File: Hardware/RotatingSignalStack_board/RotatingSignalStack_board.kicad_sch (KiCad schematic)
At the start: 42 parts, among them J1 8P8C_LED_Shielded, Q9 Q_PMOS_DGS, SW1 SW_Push, SW2 SW_Push, U1 OKI, U3 Teensy4.1_DEV-16771, U4 TSR_1-2450, U5 LSM303C

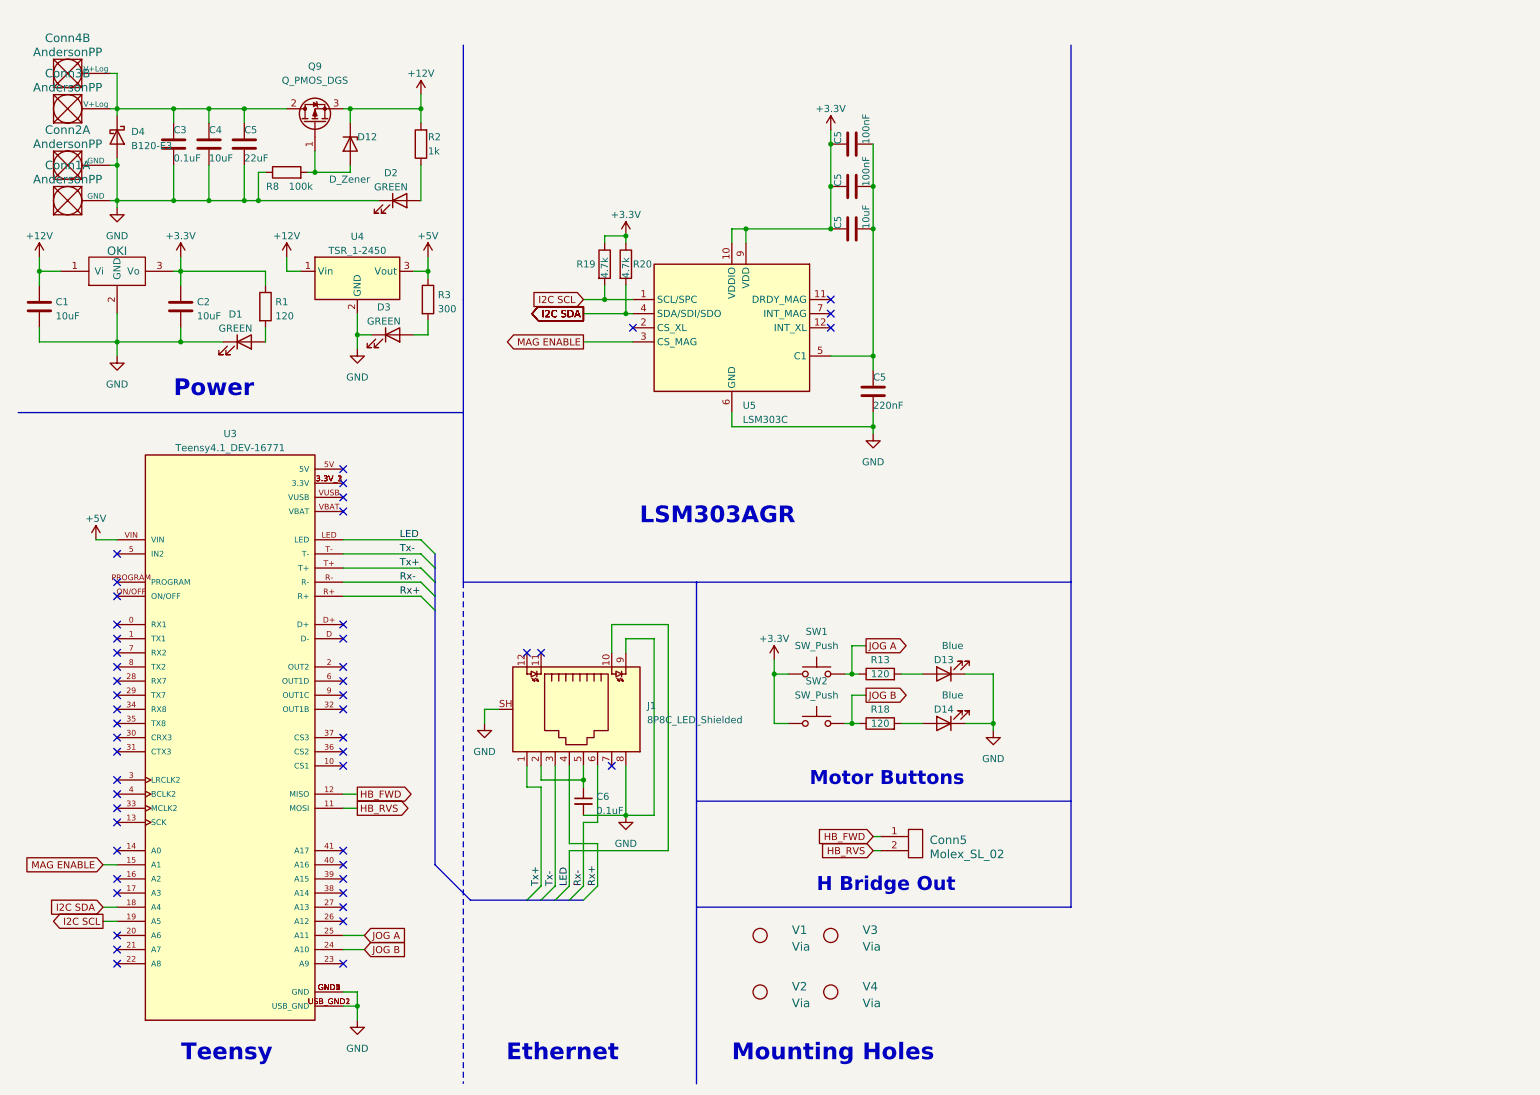
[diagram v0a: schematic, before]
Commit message: schematic changes, ethernet bus del, still have anderson issues, changed so VDDIO and VDD for compass chip are controlled by teensy outputs for startup seq to be possbile
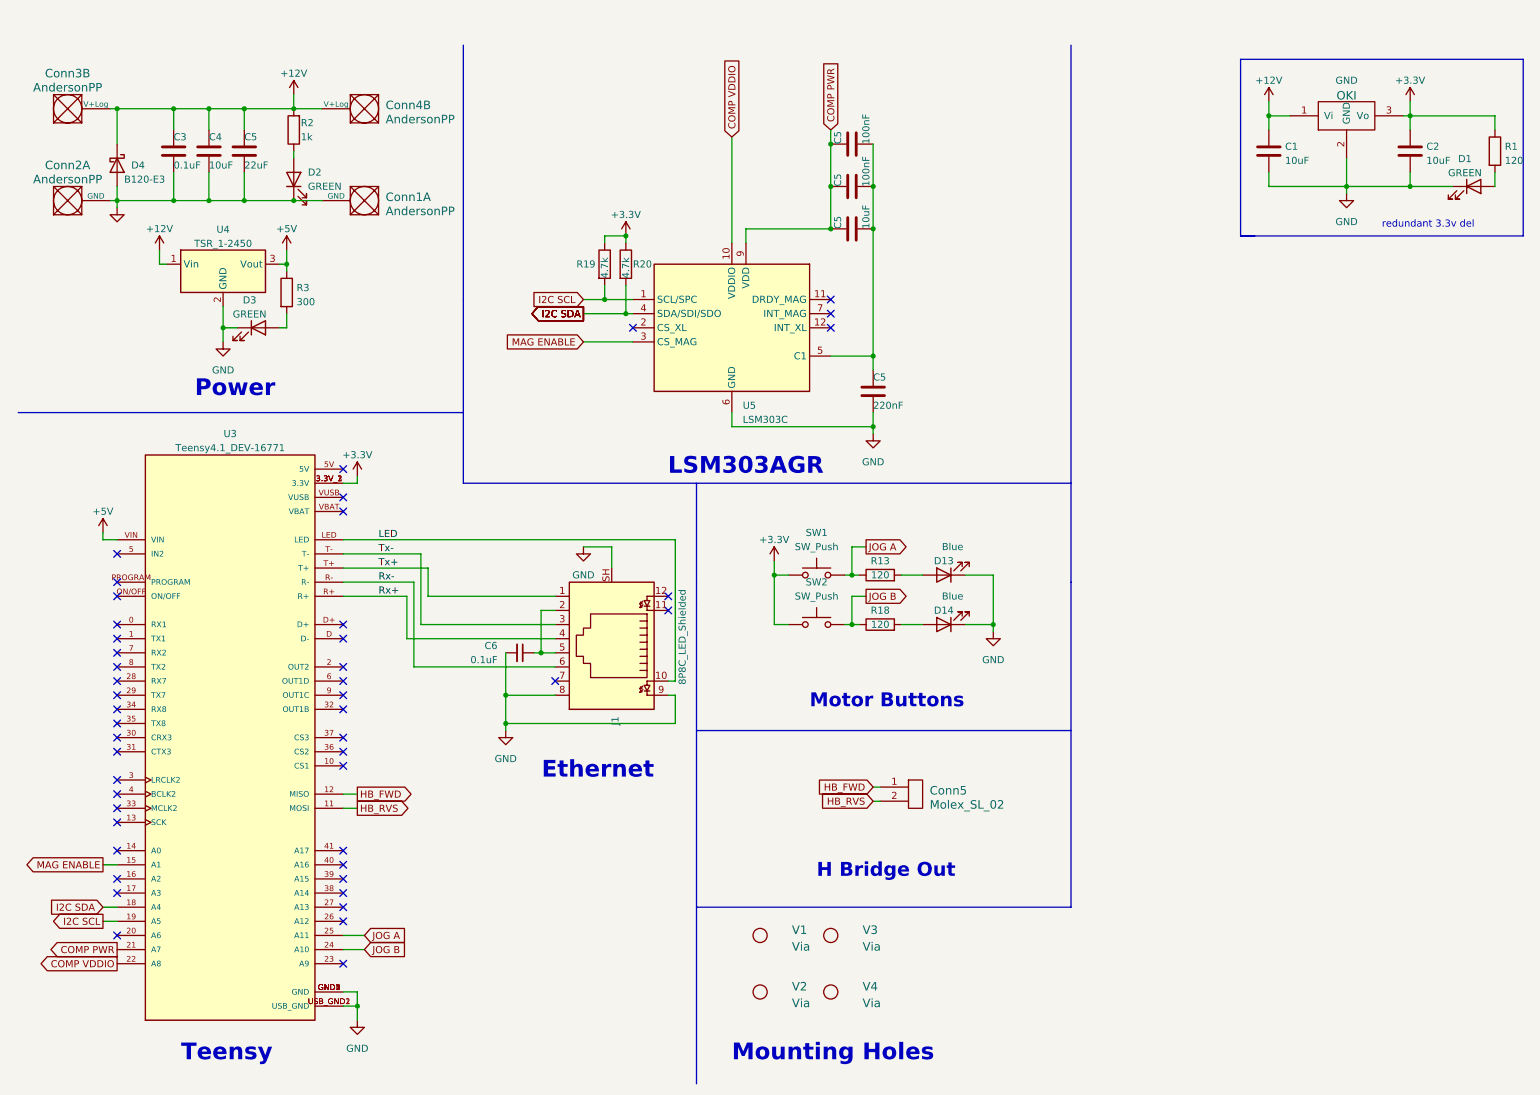
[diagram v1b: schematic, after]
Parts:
- removed D12: D_Zener, Package_TO_SOT_SMD:SOT-23-3, symbol Device:D_Zener
- removed Q9: Q_PMOS_DGS, Package_TO_SOT_SMD:TO-252-3_TabPin2, symbol Device:Q_PMOS_GDS
- removed R8: 100k, Resistor_SMD:R_0603_1608Metric_Pad0.98x0.95mm_HandSolder, symbol Device:R
- J1: footprint (none) -> MRDT_Connectors:RJ45_Teensy
- U3: footprint MODULE_DEV-16771 -> MRDT_Shields:Teensy_4_1_Ethernet
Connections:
- net +12V: now also C3.1, C4.1, C5.1, Conn3.2 (V+Log), Conn4.2 (V+Log), D4.1 (K)
- net +3.3V: now also U3.3.3V_1 (3.3V), U3.3.3V_2 (3.3V), U3.3.3V_3 (3.3V); no longer C5.1, C5.1, C5.1, U5.10 (VDDIO), U5.9 (VDD)
- net COMP PWR: now reaches U3.21 (A7)
- net COMP PWR: now also C5.1, C5.1, C5.1, U5.9 (VDD)
- net COMP VDDIO: now reaches U3.22 (A8)
- net COMP VDDIO: now also U5.10 (VDDIO)
- no-connect marks 50 -> 47
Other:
- note added: "redundant 3.3v del"
- moved on the sheet: C1, C2, C3, C4, C5, C6, Conn1A, Conn2A, Conn4B, Conn5, D1, D13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

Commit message: first update of changes from schem review, changes need double checked. BOM is generated in /manufacturing but needs filled out
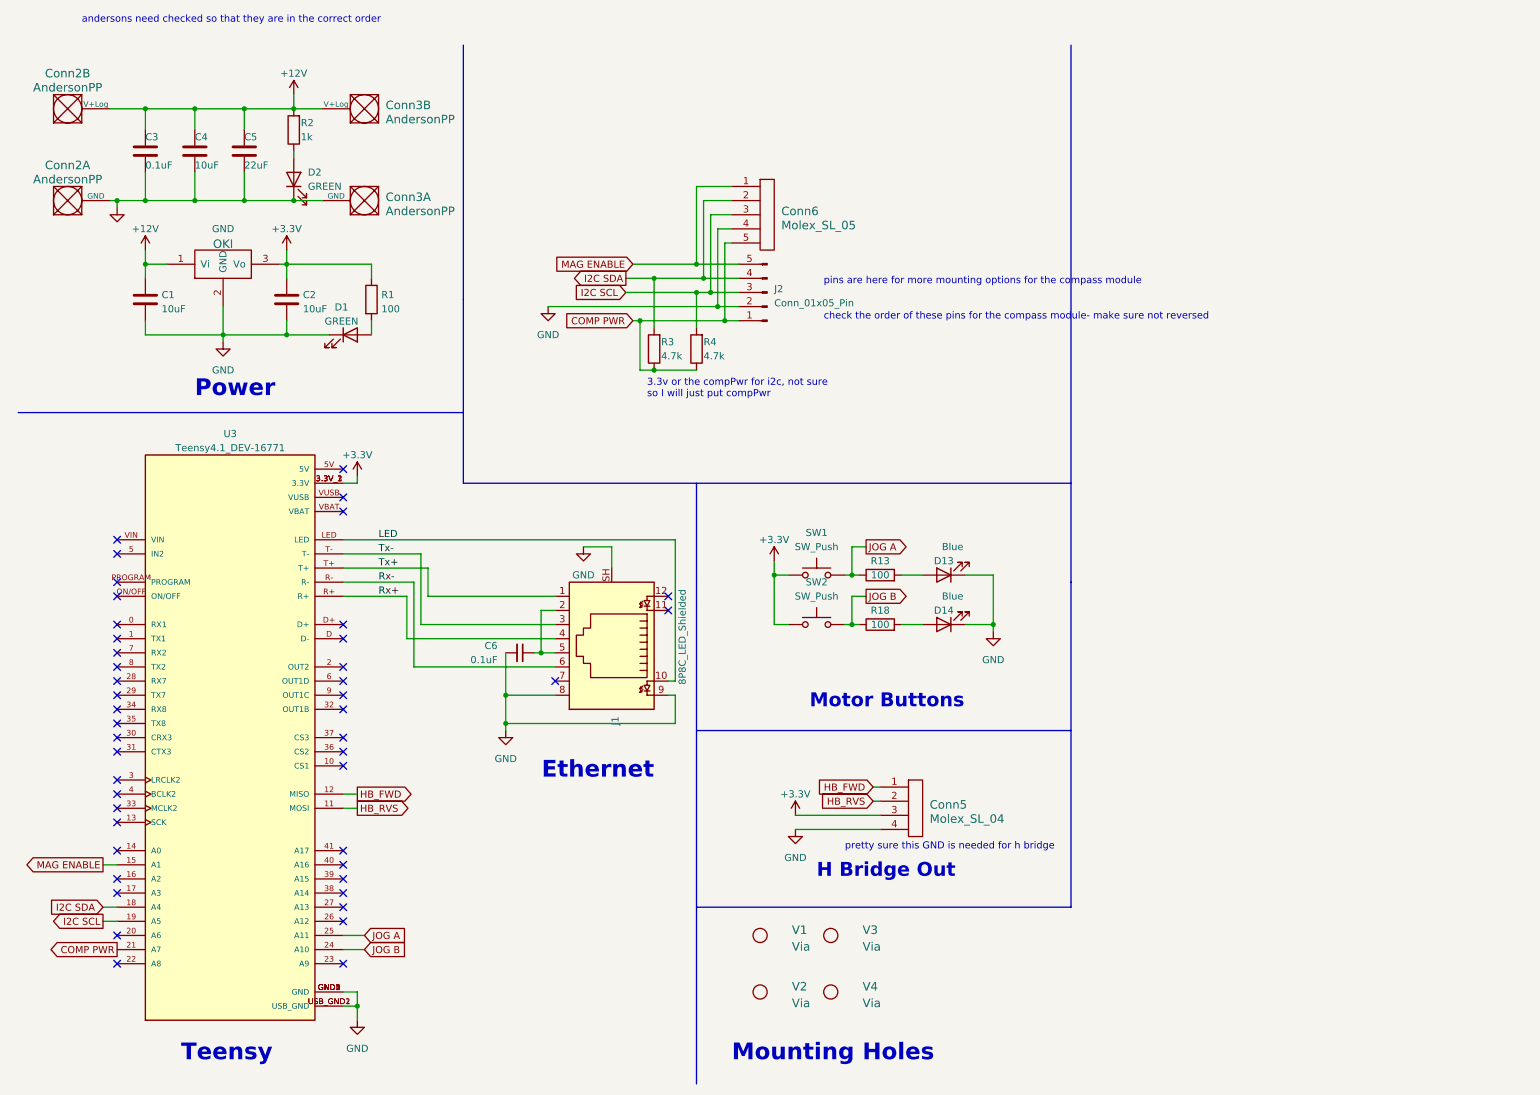
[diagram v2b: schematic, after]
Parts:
- removed C5 (x2): 100nF, Capacitor_SMD:C_0603_1608Metric_Pad1.08x0.95mm_HandSolder, symbol Device:C
- removed C5: 220nF, Capacitor_SMD:C_0603_1608Metric_Pad1.08x0.95mm_HandSolder, symbol Device:C
- removed C5: 10uF, Capacitor_SMD:C_0603_1608Metric_Pad1.08x0.95mm_HandSolder, symbol Device:C
- removed Conn5: Molex_SL_02, MRDT_Connectors:MOLEX_SL_02_Horizontal, symbol MRDT_Connectors:Molex_SL_02
- removed D3: GREEN, Diode_SMD:D_0603_1608Metric_Pad1.05x0.95mm_HandSolder, symbol Device:LED
- removed D4: B120-E3, Diode_SMD:D_SMA, symbol Diode:B120-E3
- removed R19, R20: 4.7k, Resistor_SMD:R_0603_1608Metric_Pad0.98x0.95mm_HandSolder, symbol Device:R
- removed U4: TSR_1-2450, MRDT_Devices:TSR_1-2433, symbol Regulator_Switching:TSR_1-2450
- removed U5: LSM303C, Package_LGA:LGA-12_2x2mm_P0.5mm, symbol Sensor_Motion:LSM303C
- added Conn5: Molex_SL_04, MRDT_Connectors:MOLEX_SL_04_Vertical, symbol MRDT_Connectors:Molex_SL_04
- added Conn6: Molex_SL_05, MRDT_Connectors:MOLEX_SL_05_Vertical, symbol MRDT_Connectors:Molex_SL_05
- added J2: Conn_01x05_Pin, Connector_PinHeader_1.00mm:PinHeader_1x05_P1.00mm_Vertical, symbol Connector:Conn_01x05_Pin
- added R4: 4.7k, Resistor_SMD:R_0603_1608Metric_Pad0.98x0.95mm_HandSolder, symbol Device:R
- R1, R13, R18: value 120 -> 100
- R3: value 300 -> 4.7k
- renumbered Conn3 to Conn2, Conn4 to Conn3, Conn1 to Conn3
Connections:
- net +3.3V: now also Conn5.3
- net COMP PWR: now also R3.1, Conn6.5, J2.1 (Pin_1), R4.1
- net GND: now also Conn5.4, Conn6.4, J2.2 (Pin_2)
- net HB_FWD: now also Conn5.1
- net HB_RVS: now also Conn5.2
- net I2C SCL: now also Conn6.3, J2.3 (Pin_3), R4.2
- net I2C SDA: now also R3.2, Conn6.2, J2.4 (Pin_4)
- net MAG ENABLE: now also Conn6.1, J2.5 (Pin_5)
- net +5V: no longer names the net of U3.VIN
- net +5V: no longer R3.1
- net COMP VDDIO: no longer names the net of U3.22 (A8)
- no-connect marks 47 -> 45
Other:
- note added: "3.3v or the compPwr for i2c, not sure so I will just put compPwr"
- note added: "andersons need checked so that they are in the correct order"
- note added: "check the order of these pins for the compass module- make sure not reversed"
- note added: "pins are here for more mounting options for the compass module"
- note added: "pretty sure this GND is needed for h bridge"
- note removed: "LSM303AGR"
- note removed: "redundant 3.3v del"
- moved on the sheet: C1, C2, C3, C4, D1, R1

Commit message: changes layout reveiw 1
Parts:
- removed Conn5: Molex_SL_04, MRDT_Connectors:MOLEX_SL_04_Vertical, symbol MRDT_Connectors:Molex_SL_04
- added Conn1: Molex_SL_03, MRDT_Connectors:MOLEX_SL_03_Vertical, symbol MRDT_Connectors:Molex_SL_03
- added R5: 0, Jumper:SolderJumper-2_P1.3mm_Open_RoundedPad1.0x1.5mm, symbol Device:R
- J2: footprint Connector_PinHeader_1.00mm:PinHeader_1x05_P1.00mm_Vertical -> Connector_PinHeader_2.54mm:PinHeader_1x05_P2.54mm_Vertical
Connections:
- net +3.3V: now also Conn1.3, R5.1
- net HB_FWD: now also Conn1.1
- net HB_RVS: now also Conn1.2
- net MAG ENABLE: now also R5.2
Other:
- note added: "3.3v - 0 ohm resistor - solder jumper optional power option for Compass module"
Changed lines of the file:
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@@
+    (stroke (width 0) (type default))
+  )
+  (wire (pts (xy 120.65 50.8) (xy 133.35 50.8))
     (stroke (width 0) (type default))
   )
@@
     (stroke (width 0) (type default))
   )
+  (wire (pts (xy 106.68 46.99) (xy 109.22 46.99))
+    (stroke (width 0) (type default))
+  )
   (wire (pts (xy 26.67 166.37) (xy 29.21 166.37))
     (stroke (width 0) (type default))
@@
     (stroke (width 0) (type default))
   )
+  (wire (pts (xy 120.65 46.99) (xy 116.84 46.99))
+    (stroke (width 0) (type default))
+  )
   (wire (pts (xy 105.41 113.03) (xy 105.41 120.65))
     (stroke (width 0) (type default))
@@
     (stroke (width 0) (type default))
   )
-  (wire (pts (xy 151.13 152.4) (xy 166.37 152.4))
-    (stroke (width 0) (type default))
-  )
   (wire (pts (xy 66.04 22.86) (xy 60.96 22.86))
     (stroke (width 0) (type default))
   )
-  (wire (pts (xy 121.92 50.8) (xy 133.35 50.8))
-    (stroke (width 0) (type default))
-  )
   (wire (pts (xy 59.69 48.26) (xy 59.69 50.8))
     (stroke (width 0) (type default))
@@
     (stroke (width 0) (type default))
   )
+  (wire (pts (xy 120.65 46.99) (xy 120.65 50.8))
+    (stroke (width 0) (type default))
+  )
   (wire (pts (xy 99.06 134.62) (xy 99.06 133.35))
     (stroke (width 0) (type default))
@@
   )
   (wire (pts (xy 69.85 110.49) (xy 81.28 110.49))
+    (stroke (width 0) (type default))
+  )
+  (wire (pts (xy 106.68 45.72) (xy 106.68 46.99))
     (stroke (width 0) (type default))
   )
@@
   (text "Motor Buttons" (at 153.67 130.81 0)
     (effects (font (size 2.5 2.5) (thickness 0.5) bold) (justify left bottom))
+  )
+  (text "3.3v - 0 ohm resistor - solder jumper\noptional power option for Compass module"
+    (at 104.14 31.75 0)
+    (effects (font (size 1.27 1.27)) (justify left bottom))
   )
   (text "H Bridge Out" (at 154.94 161.29 0)
@@
     )
   )
-  (global_label "MAG ENABLE" (shape input) (at 121.92 50.8 180) (fields_autoplaced)
+  (global_label "MAG ENABLE" (shape input) (at 120.65 50.8 180) (fields_autoplaced)
     (effects (font (size 1.27 1.27)) (justify right))
-    (property "Intersheetrefs" "${INTERSHEET_REFS}" (at 107.427 50.8 0)
+    (property "Intersheetrefs" "${INTERSHEET_REFS}" (at 106.157 50.8 0)
       (effects (font (size 1.27 1.27)) (justify right) hide)
     )
@@
       (effects (font (size 1.27 1.27)) (justify right))
     )
-    (property "Footprint" "Connector_PinHeader_1.00mm:PinHeader_1x05_P1.00mm_Vertical" (at 146.05 55.88 0)
+    (property "Footprint" "Connector_PinHeader_2.54mm:PinHeader_1x05_P2.54mm_Vertical" (at 146.05 55.88 0)
       (effects (font (size 1.27 1.27)) hide)
     )
@@
     )
   )
-  (symbol (lib_id "MRDT_Connectors:Molex_SL_04") (at 171.45 153.67 0) (unit 1)
-    (in_bom yes) (on_board yes) (dnp no) (fields_autoplaced)
-    (property "Reference" "Conn5" (at 175.26 147.955 0)
+  (symbol (lib_id "MRDT_Connectors:Molex_SL_03") (at 171.45 151.13 0) (unit 1)
+    (in_bom yes) (on_board yes) (dnp no) (fields_autoplaced)
+    (property "Reference" "Conn1" (at 175.26 146.685 0)
       (effects (font (size 1.524 1.524)) (justify left))
     )
-    (property "Value" "Molex_SL_04" (at 175.26 150.495 0)
+    (property "Value" "Molex_SL_03" (at 175.26 149.225 0)
       (effects (font (size 1.524 1.524)) (justify left))
     )
-    (property "Footprint" "MRDT_Connectors:MOLEX_SL_04_Vertical" (at 171.45 153.67 0)
-      (effects (font (size 1.524 1.524)) hide)
-    )
-    (property "Datasheet" "" (at 171.45 153.67 0)
+    (property "Footprint" "MRDT_Connectors:MOLEX_SL_03_Vertical" (at 171.45 151.13 0)
+      (effects (font (size 1.524 1.524)) hide)
+    )
+    (property "Datasheet" "" (at 171.45 151.13 0)
       (effects (font (size 1.524 1.524)) hide)
     )
@@
     (pin "2")
     (pin "3")
-    (pin "4")
-    (instances
-      (project "RotatingSignalStack_board"
-        (path "/28faf80f-0d43-4c6f-8a15-62300b76c48c"
-          (reference "Conn5") (unit 1)
+    (instances
+      (project "RotatingSignalStack_board"
+        (path "/28faf80f-0d43-4c6f-8a15-62300b76c48c"
+          (reference "Conn1") (unit 1)
         )
       )
@@
     )
   )
+  (symbol (lib_id "Device:R") (at 113.03 46.99 90) (unit 1)
+    (in_bom yes) (on_board yes) (dnp no)
+    (property "Reference" "R5" (at 113.03 44.45 90)
+      (effects (font (size 1.27 1.27)))
+    )
+    (property "Value" "0" (at 113.03 46.99 90)
+      (effects (font (size 1.27 1.27)))
+    )
+    (property "Footprint" "Jumper:SolderJumper-2_P1.3mm_Open_RoundedPad1.0x1.5mm" (at 113.03 48.768 90)
+      (effects (font (size 1.27 1.27)) hide)
+    )
+    (property "Datasheet" "~" (at 113.03 46.99 0)
+      (effects (font (size 1.27 1.27)) hide)
+    )
+    (pin "1")
+    (pin "2")
+    (instances
+      (project "RotatingSignalStack_board"
+        (path "/28faf80f-0d43-4c6f-8a15-62300b76c48c"
+          (reference "R5") (unit 1)
+        )
+      )
+      (project ""
+        (path "/2b2b0a19-248c-458c-9c9a-f0667cfe3a76"
+          (reference "R13") (unit 1)
+        )
+      )
+    )
+  )
   (symbol (lib_id "Switch:SW_Push") (at 154.94 115.57 0) (unit 1)
     (in_bom yes) (on_board yes) (dnp no) (fields_autoplaced)
@@
         (path "/2b2b0a19-248c-458c-9c9a-f0667cfe3a76"
           (reference "V1") (unit 1)
+        )
+      )
+    )
+  )
+  (symbol (lib_id "power:+3.3V") (at 106.68 45.72 0) (unit 1)
+    (in_bom yes) (on_board yes) (dnp no) (fields_autoplaced)
+    (property "Reference" "#PWR02" (at 106.68 49.53 0)
+      (effects (font (size 1.27 1.27)) hide)
+    )
+    (property "Value" "+3.3V" (at 106.68 41.91 0)
+      (effects (font (size 1.27 1.27)))
+    )
+    (property "Footprint" "" (at 106.68 45.72 0)
+      (effects (font (size 1.27 1.27)) hide)
+    )
+    (property "Datasheet" "" (at 106.68 45.72 0)
+      (effects (font (size 1.27 1.27)) hide)
+    )
+    (pin "1")
+    (instances
+      (project "RotatingSignalStack_board"
+        (path "/28faf80f-0d43-4c6f-8a15-62300b76c48c"
+          (reference "#PWR02") (unit 1)
         )
       )
@@
         )
       )
-    )
-  )
-  (symbol (lib_id "power:GND") (at 151.13 152.4 0) (unit 1)
-    (in_bom yes) (on_board yes) (dnp no) (fields_autoplaced)
-    (property "Reference" "#PWR02" (at 151.13 158.75 0)
-      (effects (font (size 1.27 1.27)) hide)
-    )
-    (property "Value" "GND" (at 151.13 157.48 0)
-      (effects (font (size 1.27 1.27)))
-    )
-    (property "Footprint" "" (at 151.13 152.4 0)
-      (effects (font (size 1.27 1.27)) hide)
-    )
-    (property "Datasheet" "" (at 151.13 152.4 0)
-      (effects (font (size 1.27 1.27)) hide)
-    )
-    (pin "1")
-    (instances
-      (project "RotatingSignalStack_board"
-        (path "/28faf80f-0d43-4c6f-8a15-62300b76c48c"
-          (reference "#PWR02") (unit 1)
-        )
-      )

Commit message: Minor layout changes
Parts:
- R5: footprint Jumper:SolderJumper-2_P1.3mm_Open_RoundedPad1.0x1.5mm -> Resistor_SMD:R_0603_1608Metric_Pad0.98x0.95mm_HandSolder
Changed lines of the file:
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@@
       (effects (font (size 1.27 1.27)))
     )
-    (property "Footprint" "Jumper:SolderJumper-2_P1.3mm_Open_RoundedPad1.0x1.5mm" (at 113.03 48.768 90)
+    (property "Footprint" "Resistor_SMD:R_0603_1608Metric_Pad0.98x0.95mm_HandSolder" (at 113.03 48.768 90)
       (effects (font (size 1.27 1.27)) hide)
     )
